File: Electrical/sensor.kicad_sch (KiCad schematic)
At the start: 51 parts, among them IC1 ADS131M08, J10 Conn_01x02, J11 Conn_01x05, J12 Conn_01x02, J13 Conn_01x02, J5 Conn_01x05, J6 Conn_01x05, J7 Conn_01x02, J8 Conn_01x02, J9 Conn_01x02, K1 Relay_SPDT, K2 Relay_SPDT, Q1 IRFZ44N, Q2 IRFZ44N, U6 ADR4533, Y3 20kHz Crystal

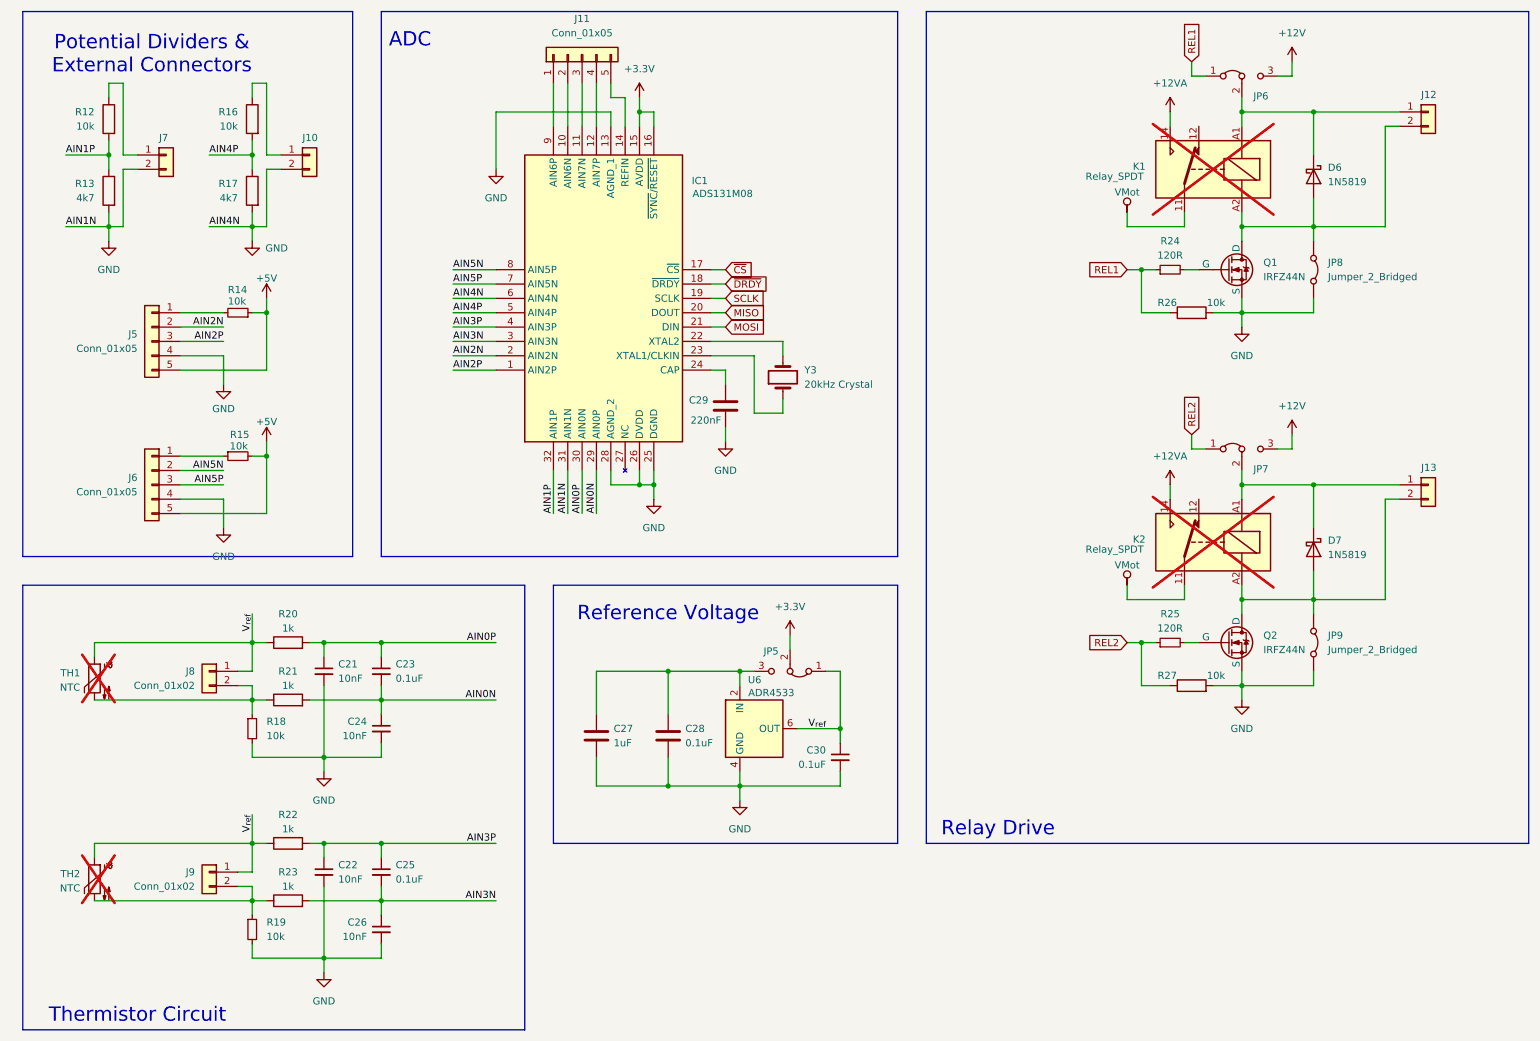
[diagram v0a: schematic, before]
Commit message: Replaced SN65HVD230 with MCP2562
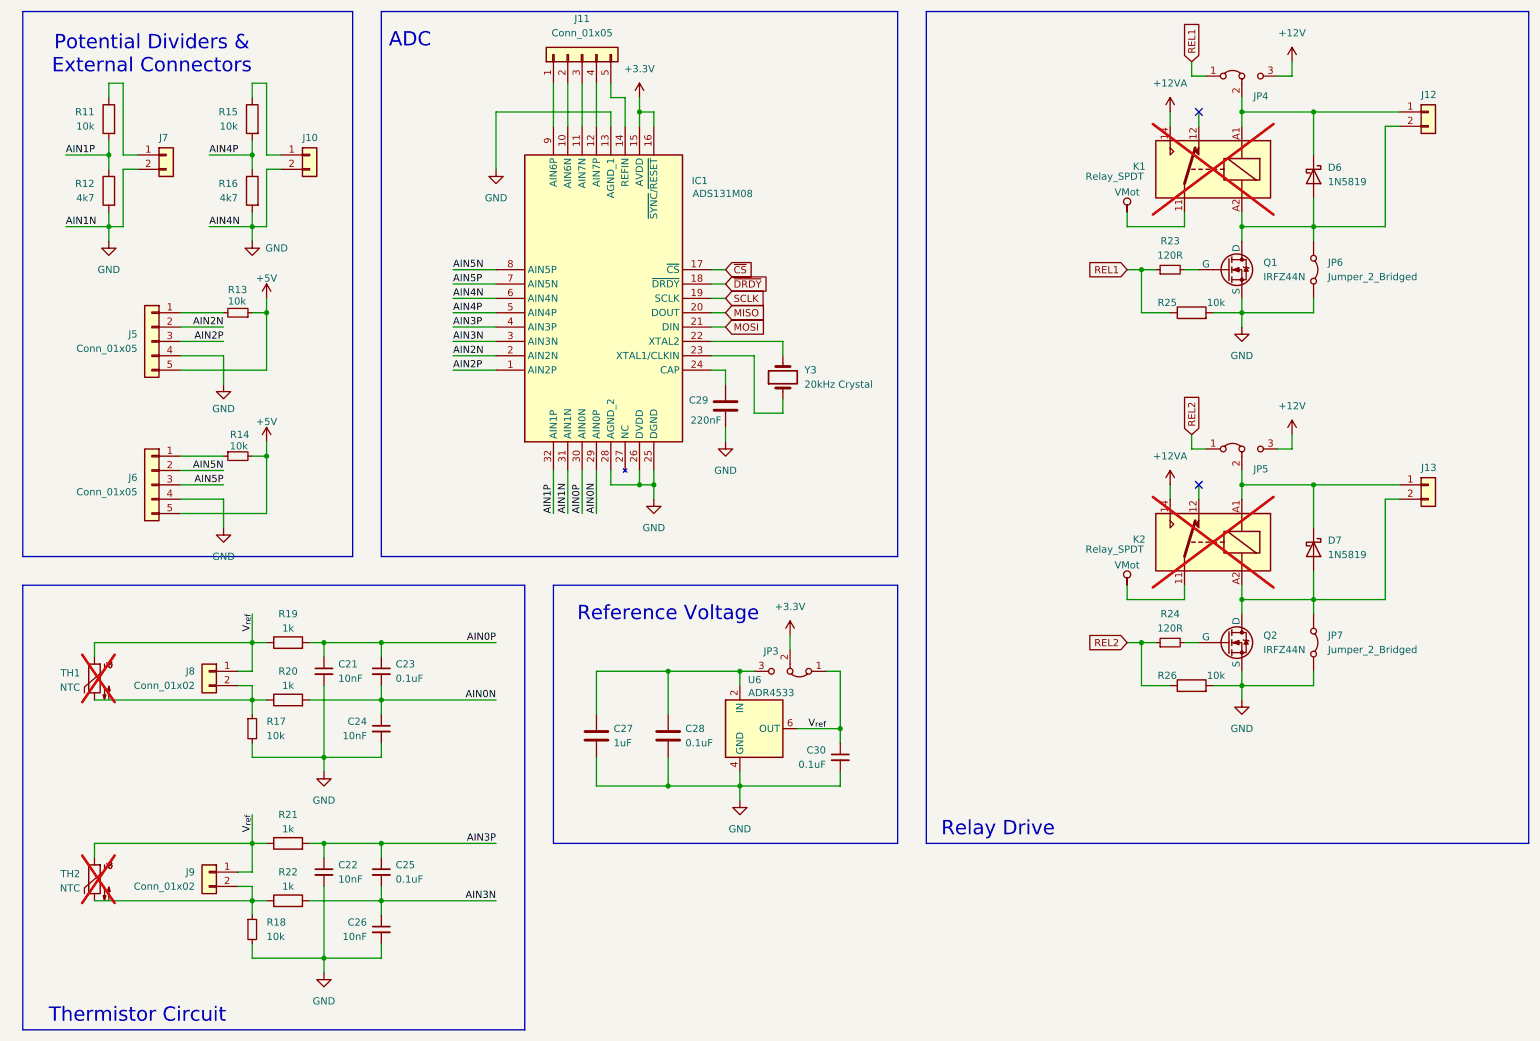
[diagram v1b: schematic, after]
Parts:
- renumbered JP5 to JP3, JP6 to JP4, JP7 to JP5, JP8 to JP6, JP9 to JP7, R12 to R11, R13 to R12, R14 to R13, R15 to R14, R16 to R15, R17 to R16, R18 to R17, R19 to R18, R20 to R19, R21 to R20, R22 to R21, R23 to R22, R24 to R23, R25 to R24, R26 to R25, R27 to R26
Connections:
- no-connect marks 0 -> 2
